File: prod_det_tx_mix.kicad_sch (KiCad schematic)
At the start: 0 parts

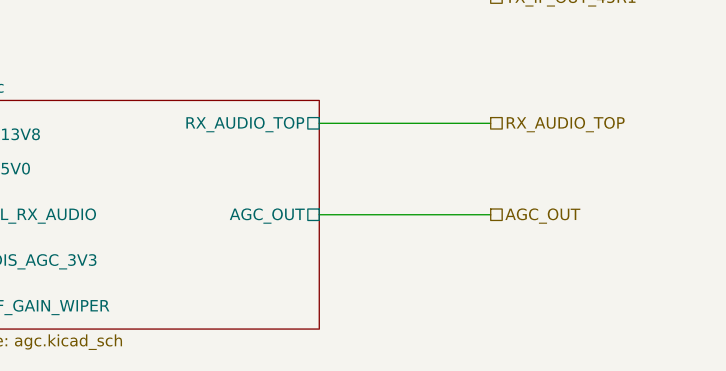
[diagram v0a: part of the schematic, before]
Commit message: trx_mobo_concept_2_B. Change design to use a dedicated 8V supply for the 2SC3357 parts. Add S-Meter connector. Change mic connector to 3 pins and add 8V sopower supply to pin 3.
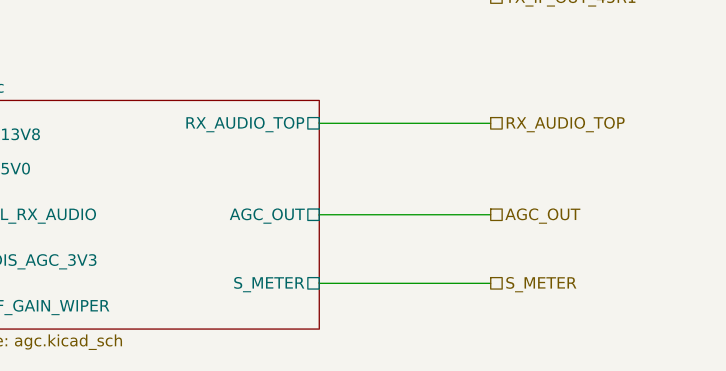
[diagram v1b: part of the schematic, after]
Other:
- sheet agc ports: added S_METER; removed none
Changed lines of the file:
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@@
   (title_block
     (title "Audio and AGC Amplifiers")
-    (rev "X1")
+    (rev "B")
     (company "WA6ZFT")
   )
@@
     (stroke (width 0) (type default) (color 0 0 0 0))
   )
+  (wire (pts (xy 165.1 57.15) (xy 139.7 57.15))
+    (stroke (width 0) (type default) (color 0 0 0 0))
+  )
+  (wire (pts (xy 165.1 96.52) (xy 130.81 96.52))
+    (stroke (width 0) (type default) (color 0 0 0 0))
+  )
+  (wire (pts (xy 139.7 57.15) (xy 139.7 36.83))
+    (stroke (width 0) (type default) (color 0 0 0 0))
+  )
+  (wire (pts (xy 157.48 30.48) (xy 157.48 40.64))
+    (stroke (width 0) (type default) (color 0 0 0 0))
+  )
+  (wire (pts (xy 52.07 63.5) (xy 33.02 63.5))
+    (stroke (width 0) (type default) (color 0 0 0 0))
+  )
+  (wire (pts (xy 135.89 45.72) (xy 33.02 45.72))
+    (stroke (width 0) (type default) (color 0 0 0 0))
+  )
+  (wire (pts (xy 33.02 30.48) (xy 157.48 30.48))
+    (stroke (width 0) (type default) (color 0 0 0 0))
+  )
   (wire (pts (xy 203.2 91.44) (xy 222.25 91.44))
     (stroke (width 0) (type default) (color 0 0 0 0))
   )
-  (wire (pts (xy 165.1 57.15) (xy 139.7 57.15))
-    (stroke (width 0) (type default) (color 0 0 0 0))
-  )
-  (wire (pts (xy 165.1 96.52) (xy 130.81 96.52))
-    (stroke (width 0) (type default) (color 0 0 0 0))
-  )
-  (wire (pts (xy 139.7 57.15) (xy 139.7 36.83))
-    (stroke (width 0) (type default) (color 0 0 0 0))
-  )
-  (wire (pts (xy 157.48 30.48) (xy 157.48 40.64))
-    (stroke (width 0) (type default) (color 0 0 0 0))
-  )
-  (wire (pts (xy 52.07 63.5) (xy 33.02 63.5))
-    (stroke (width 0) (type default) (color 0 0 0 0))
-  )
-  (wire (pts (xy 135.89 45.72) (xy 33.02 45.72))
-    (stroke (width 0) (type default) (color 0 0 0 0))
-  )
-  (wire (pts (xy 33.02 30.48) (xy 157.48 30.48))
-    (stroke (width 0) (type default) (color 0 0 0 0))
-  )
   (wire (pts (xy 31.75 106.68) (xy 165.1 106.68))
     (stroke (width 0) (type default) (color 0 0 0 0))
@@
     (stroke (width 0) (type default) (color 0 0 0 0))
   )
+  (wire (pts (xy 203.2 109.22) (xy 222.25 109.22))
+    (stroke (width 0) (type default) (color 0 0 0 0))
+  )
   (wire (pts (xy 203.2 101.6) (xy 222.25 101.6))
     (stroke (width 0) (type default) (color 0 0 0 0))
@@
   (hierarchical_label "IF_GAIN_WIPER" (shape passive) (at 31.75 111.76 180)
     (effects (font (size 1.27 1.27)) (justify right))
+  )
+  (hierarchical_label "S_METER" (shape passive) (at 222.25 109.22 0)
+    (effects (font (size 1.27 1.27)) (justify left))
   )
   (hierarchical_label "MUTE_RX_AUDIO" (shape input) (at 33.02 30.48 180)
@@
       (effects (font (size 1.27 1.27)) (justify left))
     )
-  )
+    (pin "S_METER" passive (at 203.2 109.22 0)
+      (effects (font (size 1.27 1.27)) (justify right))
+    )
+  )
